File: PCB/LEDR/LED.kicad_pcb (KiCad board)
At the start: 2 copper layers, 70 x 70 mm, 48 parts, among them J1 Reset, J2 Wago, J3 TC2030-USB-NL-DS, J4 SPK, J5 USB-C-Socket-H, J6 RELAY, SW1 Button, U1 ICS43434_MEMS_Mic, U2 MAX98357A, U3 Relay, U4 78L05, U5 IRM-H638T/TR2, U6 ESP32-S3-MINI-1, U7 MD8942, U8 VEML6040

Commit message: Silk screen
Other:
- board text removed: "3.3V I/O"

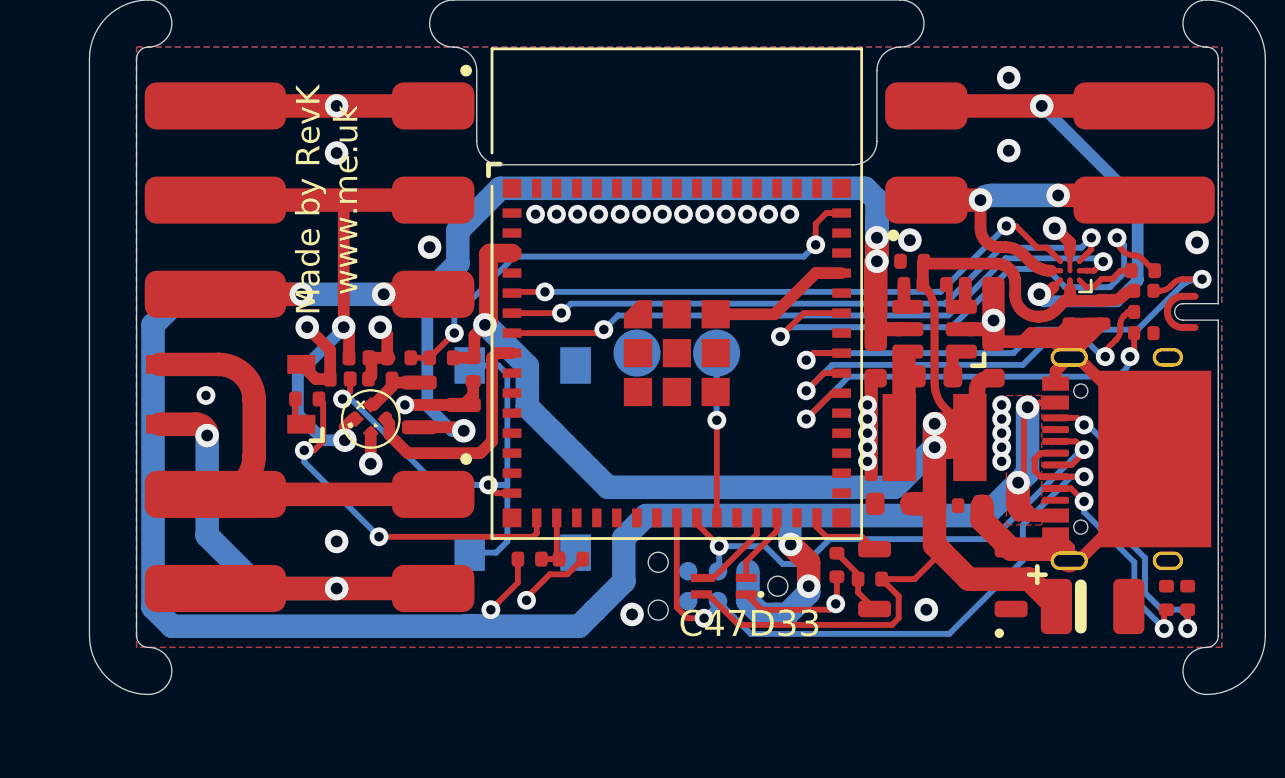
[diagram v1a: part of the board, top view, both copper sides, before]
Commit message: Changed relay logic
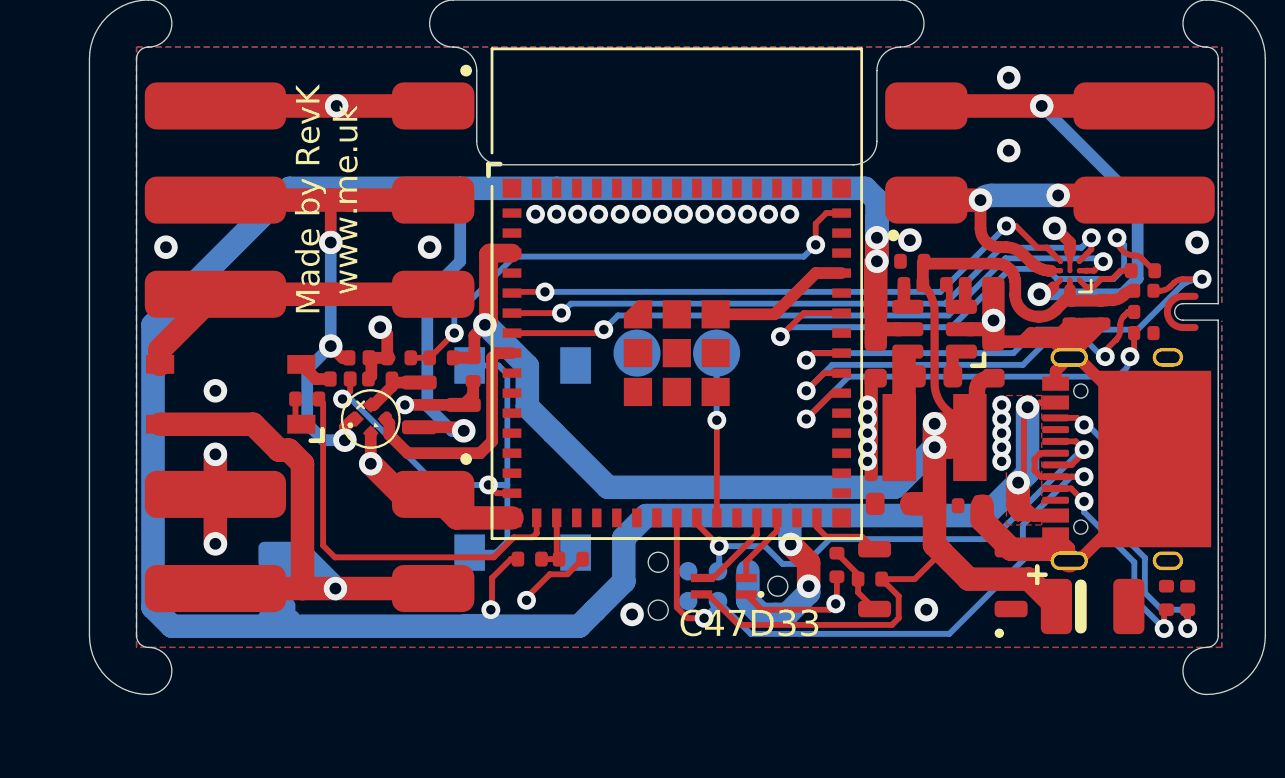
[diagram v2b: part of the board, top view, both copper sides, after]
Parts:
- added JP1: PWR, RevK:Pad_1206_0805_Bridged, B.Cu at (83.1, 105.5)
- J2: value Wago -> LED
- J6: value RELAY -> Power
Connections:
- J2 pad 3: DC -> Net-(J2-Pin_3)
- J6 pad 1: Net-(J6-Pin_1) -> GND
- U3 pad 3: Net-(J6-Pin_1) -> Net-(J2-Pin_3)
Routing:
- net Net-(J6-Pin_1): track 18.9 -> 0.00 mm
- net Net-(J2-Pin_3): track 0.00 -> 13.2 mm
- net LED2: track 33.3 -> 23.1 mm, vias 2 -> 3
- net GND: track 76.1 -> 84.3 mm
- net Net-(J6-Pin_2): track 22.2 -> 24.3 mm, vias 2 -> 1
- net RELAY: track 15.2 -> 16.7 mm, vias 2 -> 0
- net DC: track 135.4 -> 134.1 mm, vias 10 -> 8
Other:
- board text added: "EXTERNAL"
- board text added: "SWITCHED"
- board text added: "USB"

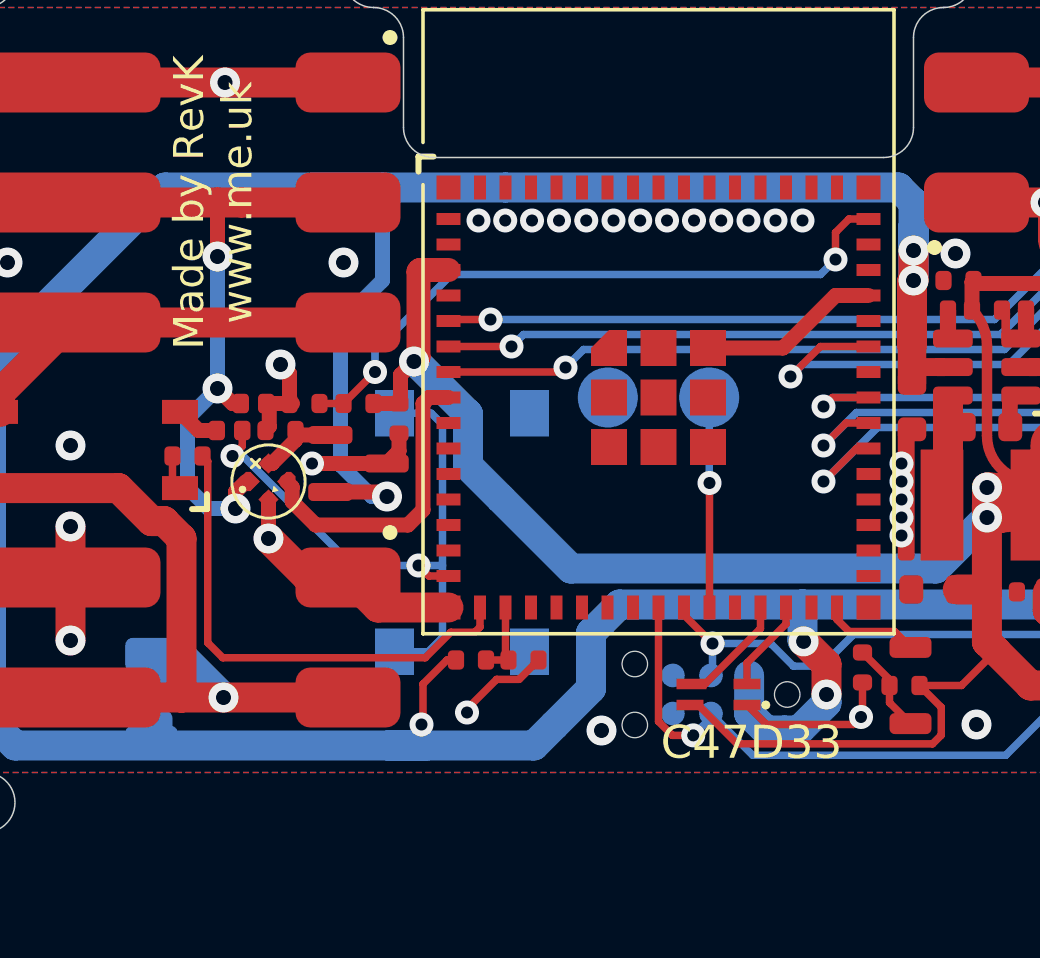
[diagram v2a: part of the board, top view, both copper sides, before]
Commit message: Changed so no level shifter as forces RGB not RGBW
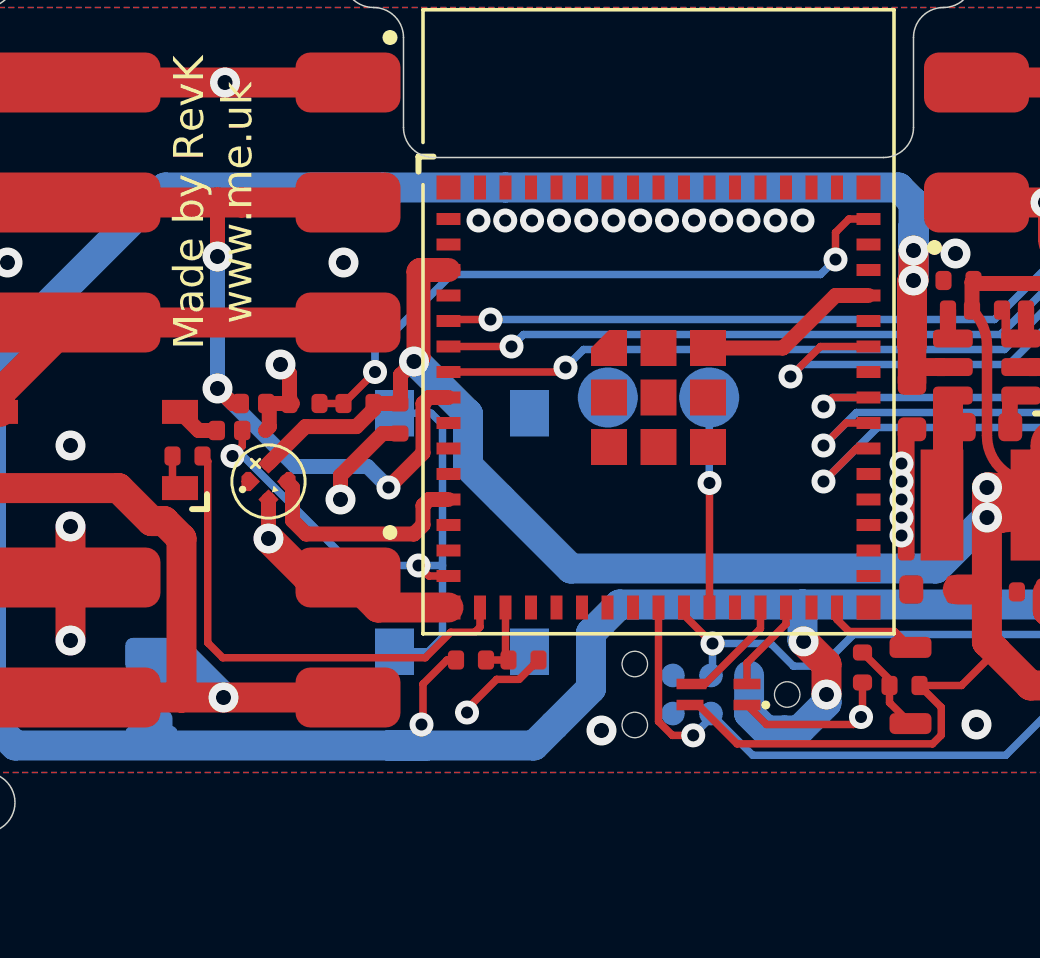
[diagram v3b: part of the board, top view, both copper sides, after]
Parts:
- removed C15: 100nF, RevK:C_0402
- removed U4: 78L05, RevK:SOT-23
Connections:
- D1 pad 1: LED2 -> unconnected-(D1-O-Pad1)_1
- D1 pad 2: Net-(D1-+) -> +3V3
- U6 pad 12: unconnected-(U6-GPIO8-Pad12) -> LED1
- U6 pad 8: LED1 -> LED2
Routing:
- net DC: track 134.1 -> 120.4 mm, vias 8 -> 7
- net LED2: track 23.1 -> 27.7 mm
- net +3V3: track 75.3 -> 79.8 mm
- net Net-(D1-+): track 2.77 -> 0.00 mm
- net LED1: track 10.1 -> 7.63 mm
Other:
- board text added: "5V- 35V"
- board text added: "8"
- board text added: "I/O 3.3V"

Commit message: Tidy
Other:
- board text added: "QRQR"

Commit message: Started on new coaster
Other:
- board text removed: "QRQR"

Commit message: Name
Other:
- board text added: "LED"
- board text added: "USB ONLY IF NOT EXTERNAL POWER"
- board text removed: "USB ONLY IF NOT EXTERFNAL POWER"

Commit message: New image files
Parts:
- removed REF**: Shadow, RevK:Shadow
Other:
- copper layers 2 -> 4
